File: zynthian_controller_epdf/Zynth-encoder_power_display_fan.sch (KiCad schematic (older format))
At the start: 41 parts, among them J3 40HAT, Q1 DMG2305UX, Q2 DMMT5401, Q3 AOD4184A, U2 CAT24C32, U3 MCP23017_SS

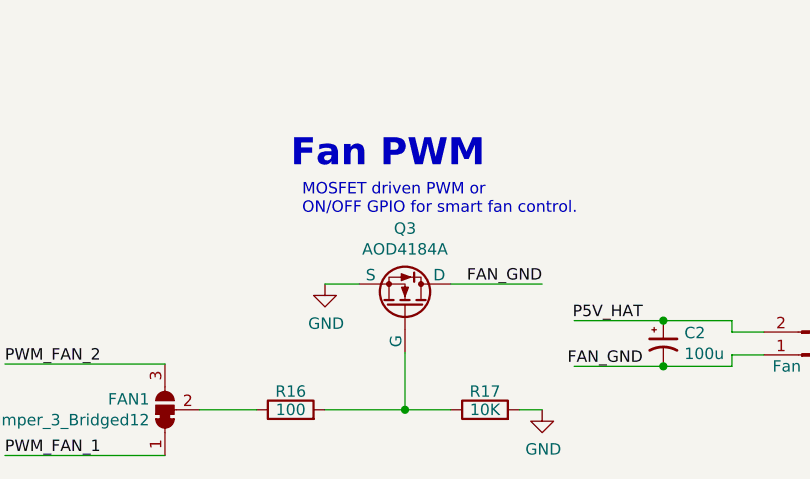
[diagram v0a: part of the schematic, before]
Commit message: Corrections before production.
Optimized and tested for submit
Manually corrected R12,18,19 as well as pin 1 orientations.
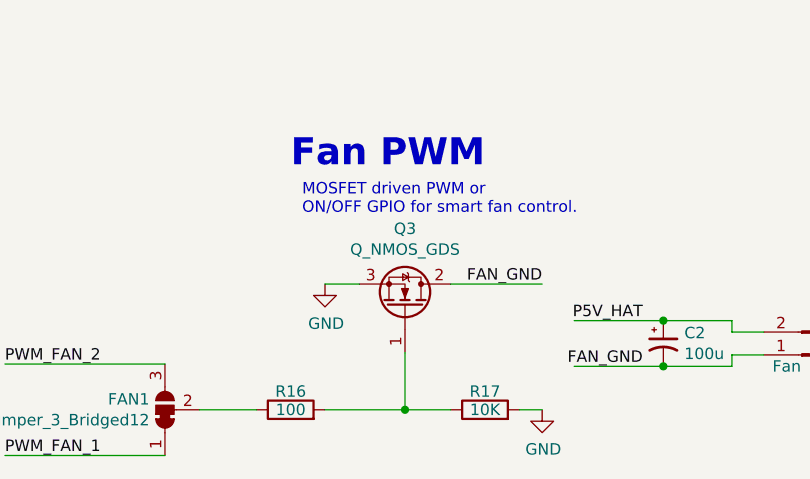
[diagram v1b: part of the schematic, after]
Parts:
- removed Q3: AOD4184A, Package_TO_SOT_SMD:TO-252-2, symbol Transistor_FET:AOD4184A
- added Q3: Q_NMOS_GDS, Package_TO_SOT_SMD:TO-252-2, symbol Device:Q_NMOS_GDS
- C2: footprint Capacitor_Tantalum_SMD:CP_EIA-7343-30_AVX-N -> Capacitor_Tantalum_SMD:CP_EIA-3528-15_AVX-H; LCSC C139578 -> C16133
- D5: LCSC C72044 -> C2286; MFG PART 19-217/R6C-AL1M2VY/3T -> (none)
- R10, R15, R17: LCSC C167144 -> C25804
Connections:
- net FAN_GND: now also Q3.2 (D)
- net GND: now also Q3.3 (S)
- net at R16.2, R17.1: now also Q3.1 (G)

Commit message: Final Changes before production
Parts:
- added R20: 100K, Resistor_SMD:R_0603_1608Metric, symbol Device:R
- C1: MFG PART CC0603KRX7R9BB104 -> (none)
- C2: MFG PART 20TQC100MYF -> (none)
- H5, H6: Field4 Pi Zero Mounting Hole -> (none)
- PWR1: Name ACC1 -> (none)
- PWR2: Name DSPL_PWR -> (none)
- PWR3: Name Fan -> (none)
- Q1: MFG PART DMG2305UX-13 -> (none)
- Q2: MFG PART DMMT5401-7-F -> (none)
- R10, R15, R17: MFG PART 0603WAD1002T5E -> (none)
- R11: footprint Resistor_SMD:R_0402_1005Metric -> Resistor_SMD:R_0603_1608Metric; LCSC C25792 -> C25819; MFG PART 0402WGF4702TCE -> (none)
- R12: MFG PART 0603WAF1001T5E -> (none)
- R13, R14: MFG PART 0603WAF3901T5E -> (none)
- R16: MFG PART 0805W8F1000T5E -> (none)
- R18, R19: value 1k -> 1K; MFG PART 0603WAF1001T5E -> (none)
- SJ1: Field4 EEPROM Write Enable -> (none)
- U2: MFG PART CAT24C32WI-GT3 -> (none)
- U3: MFG PART MCP23017-E/SO -> (none)
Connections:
- net E1+: now also R20.1
- net GND: now also R20.2
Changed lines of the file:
@@
 F 3 "https://datasheet.lcsc.com/szlcsc/Uniroyal-Elec-0603WAF1001T5E_C21190.pdf" H 6130 2400 50  0001 C CNN
 F 4 "C144153" H 6130 2400 50  0001 C CNN "LCSC"
-F 5 "DMG2305UX-13" H 6130 2400 50  0001 C CNN "MFG PART"
 	1    6130 2400
 	0    -1   -1   0
@@
 F 3 "https://datasheet.lcsc.com/szlcsc/Diodes-Incorporated-DMMT5401-7-F_C154733.pdf" H 5830 3000 50  0001 L CNN
 F 4 "C154733" H 5830 3000 50  0001 C CNN "LCSC"
-F 5 "DMMT5401-7-F" H 5830 3000 50  0001 C CNN "MFG PART"
 	1    5830 3000
 	-1   0    0    1
@@
 F 3 "https://datasheet.lcsc.com/szlcsc/Diodes-Incorporated-DMMT5401-7-F_C154733.pdf" H 6430 3000 50  0001 L CNN
 F 4 "C154733" H 6430 3000 50  0001 C CNN "LCSC"
-F 5 "DMMT5401-7-F" H 6430 3000 50  0001 C CNN "MFG PART"
 	2    6430 3000
 	1    0    0    1
@@
 F 3 "https://datasheet.lcsc.com/szlcsc/1811062009_UNI-ROYAL-Uniroyal-Elec-0603WAF1002T5E_C25804.pdf" H 5730 3600 50  0001 C CNN
 F 4 "C25804" H 5730 3600 50  0001 C CNN "LCSC"
-F 5 "0603WAD1002T5E" H 5730 3600 50  0001 C CNN "MFG PART"
 	1    5730 3600
 	1    0    0    -1
@@
 F 1 "5V Power" H 11640 3140 50  0001 C CNN
 F 2 "Connector_Wire:SolderWirePad_1x02_P5.08mm_Drill1.5mm" H 11390 3040 50  0001 C CNN
-F 3 "https://www.te.com/commerce/DocumentDelivery/DDEController?Action=srchrtrv&DocNm=63951&DocType=Customer+Drawing&DocLang=English" H 11390 3040 50  0001 C CNN
+F 3 "~" H 11390 3040 50  0001 C CNN
 	1    11390 3040
 	-1   0    0    -1
@@
 F 1 "GND" H 11640 1990 50  0001 R CNN
 F 2 "Connector_Wire:SolderWirePad_1x02_P5.08mm_Drill1.5mm" H 11390 2190 50  0001 C CNN
-F 3 "https://www.te.com/commerce/DocumentDelivery/DDEController?Action=srchrtrv&DocNm=63951&DocType=Customer+Drawing&DocLang=English" H 11390 2190 50  0001 C CNN
+F 3 "~" H 11390 2190 50  0001 C CNN
 	1    11390 2190
 	-1   0    0    1
@@
 F 0 "R11" V 6610 3600 50  0000 C CNN
 F 1 "47K" V 6530 3600 50  0000 C CNN
-F 2 "Resistor_SMD:R_0402_1005Metric" V 6460 3600 50  0001 C CNN
-F 3 "https://datasheet.lcsc.com/szlcsc/Uniroyal-Elec-0402WGF4702TCE_C25792.pdf" H 6530 3600 50  0001 C CNN
-F 4 "C25792" H 6530 3600 50  0001 C CNN "LCSC"
-F 5 "0402WGF4702TCE" H 6530 3600 50  0001 C CNN "MFG PART"
+F 2 "Resistor_SMD:R_0603_1608Metric" V 6460 3600 50  0001 C CNN
+F 3 "https://datasheet.lcsc.com/szlcsc/Uniroyal-Elec-0603WAF4702T5E_C25819.pdf" H 6530 3600 50  0001 C CNN
+F 4 "C25819" H 6530 3600 50  0001 C CNN "LCSC"
 	1    6530 3600
 	1    0    0    -1
@@
 F 3 "https://datasheet.lcsc.com/szlcsc/Uniroyal-Elec-0603WAF1001T5E_C21190.pdf" H 9990 2390 50  0001 C CNN
 F 4 "C21190" H 9990 2390 50  0001 C CNN "LCSC"
-F 5 "0603WAF1001T5E" H 9990 2390 50  0001 C CNN "MFG PART"
 	1    9990 2390
 	1    0    0    1
@@
 F 2 "Jumper:SolderJumper-2_P1.3mm_Open_RoundedPad1.0x1.5mm" H 940 6030 50  0001 C CNN
 F 3 "~" H 940 6030 50  0001 C CNN
-F 4 "EEPROM Write Enable" V 810 5540 50  0000 C CNN "Field4"
 	1    940  6030
 	0    -1   -1   0
@@
 F 3 "https://datasheet.lcsc.com/szlcsc/Uniroyal-Elec-0603WAF3901T5E_C23018.pdf" H 3030 7450 50  0001 C CNN
 F 4 "C23018" H 3030 7450 50  0001 C CNN "LCSC"
-F 5 "0603WAF3901T5E" H 3030 7450 50  0001 C CNN "MFG PART"
 	1    3030 7450
 	0    1    1    0
@@
 F 3 "https://datasheet.lcsc.com/szlcsc/Uniroyal-Elec-0603WAF3901T5E_C23018.pdf" H 3030 7200 50  0001 C CNN
 F 4 "C23018" H 3030 7200 50  0001 C CNN "LCSC"
-F 5 "0603WAF3901T5E" H 3030 7200 50  0001 C CNN "MFG PART"
 	1    3030 7200
 	0    1    1    0
@@
 F 3 "https://datasheet.lcsc.com/szlcsc/ON-Semicon-ON-CAT24C32WI-GT3_C81193.pdf" H 2620 5680 50  0001 C CNN
 F 4 "C81193" H 2620 5680 50  0001 C CNN "LCSC"
-F 5 "CAT24C32WI-GT3" H 2620 5680 50  0001 C CNN "MFG PART"
 	1    2620 5680
 	1    0    0    -1
@@
 F 2 "project_footprints:NPTH_3mm_ID" H 12660 3010 60  0001 C CNN
 F 3 "~" H 12660 3010 60  0001 C CNN
-F 4 "Pi Zero Mounting Hole" H 12750 2760 50  0000 C CNN "Field4"
 	1    12760 3010
 	1    0    0    -1
@@
 F 2 "project_footprints:NPTH_3mm_ID" H 13710 3010 60  0001 C CNN
 F 3 "~" H 13710 3010 60  0001 C CNN
-F 4 "Pi Zero Mounting Hole" H 13800 2760 50  0000 C CNN "Field4"
 	1    13810 3010
 	1    0    0    -1
@@
 F 3 "https://datasheet.lcsc.com/szlcsc/1811071223_AVX-TAJB107K006RNJ_C16133.pdf" H 4120 9470 50  0001 C CNN
 F 4 "C16133" H 4120 9470 50  0001 C CNN "LCSC"
-F 5 "20TQC100MYF" H 4120 9470 50  0001 C CNN "MFG PART"
 	1    4120 9470
 	1    0    0    -1
@@
 F 3 "https://datasheet.lcsc.com/szlcsc/1811062009_UNI-ROYAL-Uniroyal-Elec-0603WAF1002T5E_C25804.pdf" H 3340 9760 50  0001 C CNN
 F 4 "C25804" H 3340 9760 50  0001 C CNN "LCSC"
-F 5 "0603WAD1002T5E" H 3340 9760 50  0001 C CNN "MFG PART"
 	1    3340 9760
 	0    -1   -1   0
@@
 F 2 "Connector_JST:JST_XH_B2B-XH-A_1x02_P2.50mm_Vertical" H 4760 9520 50  0001 C CNN
 F 3 "~" H 4760 9520 50  0001 C CNN
-F 4 "Fan" H 4860 9570 50  0000 C CNN "Name"
 	1    4760 9520
 	-1   0    0    1
@@
 F 2 "Connector_JST:JST_XH_B2B-XH-A_1x02_P2.50mm_Vertical" H 10540 3920 50  0001 C CNN
 F 3 "~" H 10540 3920 50  0001 C CNN
-F 4 "DSPL_PWR" H 10790 4020 50  0000 C CNN "Name"
 	1    10540 3920
 	-1   0    0    1
@@
 F 3 "https://datasheet.lcsc.com/szlcsc/1811062009_UNI-ROYAL-Uniroyal-Elec-0603WAF1002T5E_C25804.pdf" H 2070 6230 50  0001 C CNN
 F 4 "C25804" H 2070 6230 50  0001 C CNN "LCSC"
-F 5 "0603WAD1002T5E" H 2070 6230 50  0001 C CNN "MFG PART"
 	1    2070 6230
 	-1   0    0    1
@@
 Text Label 12330 7000 2    50   ~ 0
 GSW2
-$Comp
-L Device:R R18
-U 1 1 5E20EC4C
-P 12330 8250
-F 0 "R18" V 12230 8250 50  0000 C CNN
-F 1 "1k" V 12330 8250 50  0000 C CNN
-F 2 "Resistor_SMD:R_0603_1608Metric" V 12260 8250 50  0001 C CNN
-F 3 "https://datasheet.lcsc.com/szlcsc/Uniroyal-Elec-0603WAF1001T5E_C21190.pdf" H 12330 8250 50  0001 C CNN
-F 4 "C21190" H 12330 8250 50  0001 C CNN "LCSC"
-F 5 "0603WAF1001T5E" H 12330 8250 50  0001 C CNN "MFG PART"
-	1    12330 8250
-	0    1    1    0
-$EndComp
-$Comp
-L Interface_Expansion:MCP23017_SS U3
-U 1 1 5E01D4F6
-P 11280 7100
-F 0 "U3" H 11280 8381 50  0000 C CNN
-F 1 "MCP23017_SS" H 11280 8290 50  0000 C CNN
-F 2 "Package_SO:SOIC-28W_7.5x17.9mm_P1.27mm" H 11480 6100 50  0001 L CNN
-F 3 "http://ww1.microchip.com/downloads/en/DeviceDoc/20001952C.pdf" H 11480 6000 50  0001 L CNN
-F 4 "C47023" H 11280 7100 50  0001 C CNN "LCSC"
-F 5 "MCP23017-E/SO" H 11280 7100 50  0001 C CNN "MFG PART"
-	1    11280 7100
-	1    0    0    -1
-$EndComp
 Text Notes 9270 6940 0    50   ~ 0
 I2C Addr: \n          A0   A1   A2\n0x20: 1-2  1-2  1-2\n0x21: 2-3  1-2  1-2\n0x22: 1-2  2-3  1-2\n0x23: 2-3  2-3  1-2\n\n
@@
 F 3 "https://datasheet.lcsc.com/szlcsc/YAGEO-CC0603KRX7R9BB104_C14663.pdf" H 11780 5900 50  0001 C CNN
 F 4 "C14663" H 11780 5900 50  0001 C CNN "LCSC"
-F 5 "CC0603KRX7R9BB104" H 11780 5900 50  0001 C CNN "MFG PART"
 	1    11780 5900
 	1    0    0    -1
@@
 F 2 "Connector_JST:JST_XH_B4B-XH-A_1x04_P2.50mm_Vertical" H 7320 5730 50  0001 C CNN
 F 3 "~" H 7320 5730 50  0001 C CNN
-F 4 "ACC1" H 7420 5920 50  0000 C CNN "Name"
 	1    7320 5730
 	-1   0    0    1
@@
 P 6120 5680
 F 0 "R19" V 6220 5660 50  0000 C CNN
-F 1 "1k" V 6120 5680 50  0000 C CNN
+F 1 "1K" V 6120 5680 50  0000 C CNN
 F 2 "Resistor_SMD:R_0603_1608Metric" V 6050 5680 50  0001 C CNN
 F 3 "https://datasheet.lcsc.com/szlcsc/Uniroyal-Elec-0603WAF1001T5E_C21190.pdf" H 6120 5680 50  0001 C CNN
 F 4 "C21190" H 6120 5680 50  0001 C CNN "LCSC"
-F 5 "0603WAF1001T5E" H 6120 5680 50  0001 C CNN "MFG PART"
 	1    6120 5680
 	0    1    1    0
@@
 F 3 "https://datasheet.lcsc.com/szlcsc/Uniroyal-Elec-0805W8F1000T5E_C17408.pdf" H 2490 9760 50  0001 C CNN
 F 4 "C17408" H 2490 9760 50  0001 C CNN "LCSC"
-F 5 "0805W8F1000T5E" H 2490 9760 50  0001 C CNN "MFG PART"
 	1    2490 9760
 	0    -1   -1   0
 $EndComp
+$Comp
+L Interface_Expansion:MCP23017_SS U3
+U 1 1 5E01D4F6
+P 11280 7100
+F 0 "U3" H 11280 8381 50  0000 C CNN
+F 1 "MCP23017_SS" H 11280 8290 50  0000 C CNN
+F 2 "Package_SO:SOIC-28W_7.5x17.9mm_P1.27mm" H 11480 6100 50  0001 L CNN
+F 3 "http://ww1.microchip.com/downloads/en/DeviceDoc/20001952C.pdf" H 11480 6000 50  0001 L CNN
+F 4 "C47023" H 11280 7100 50  0001 C CNN "LCSC"
+	1    11280 7100
+	1    0    0    -1
+$EndComp
+$Comp
+L Device:R R20
+U 1 1 5E66F556
+P 12330 8390
+F 0 "R20" V 12420 8390 50  0000 C CNN
+F 1 "100K" V 12330 8390 50  0000 C CNN
+F 2 "Resistor_SMD:R_0603_1608Metric" V 12260 8390 50  0001 C CNN
+F 3 "https://datasheet.lcsc.com/szlcsc/1810201809_UNI-ROYAL-Uniroyal-Elec-0603WAF1003T5E_C25803.pdf" H 12330 8390 50  0001 C CNN
+F 4 "C25803" V 12330 8390 50  0001 C CNN "LCSC"
+	1    12330 8390
+	0    1    1    0
+$EndComp
+$Comp
+L Device:R R18
+U 1 1 5E20EC4C
+P 12330 8250
+F 0 "R18" V 12230 8250 50  0000 C CNN
+F 1 "1K" V 12330 8250 50  0000 C CNN
+F 2 "Resistor_SMD:R_0603_1608Metric" V 12260 8250 50  0001 C CNN
+F 3 "https://datasheet.lcsc.com/szlcsc/Uniroyal-Elec-0603WAF1001T5E_C21190.pdf" H 12330 8250 50  0001 C CNN
+F 4 "C21190" H 12330 8250 50  0001 C CNN "LCSC"
+	1    12330 8250
+	0    1    1    0
+$EndComp
+Wire Wire Line
+	12480 8390 12480 8250
+Connection ~ 12480 8250
+Wire Wire Line
+	12180 8390 11830 8390
+Text Label 11830 8390 0    50   ~ 0
+GND
 $EndSCHEMATC

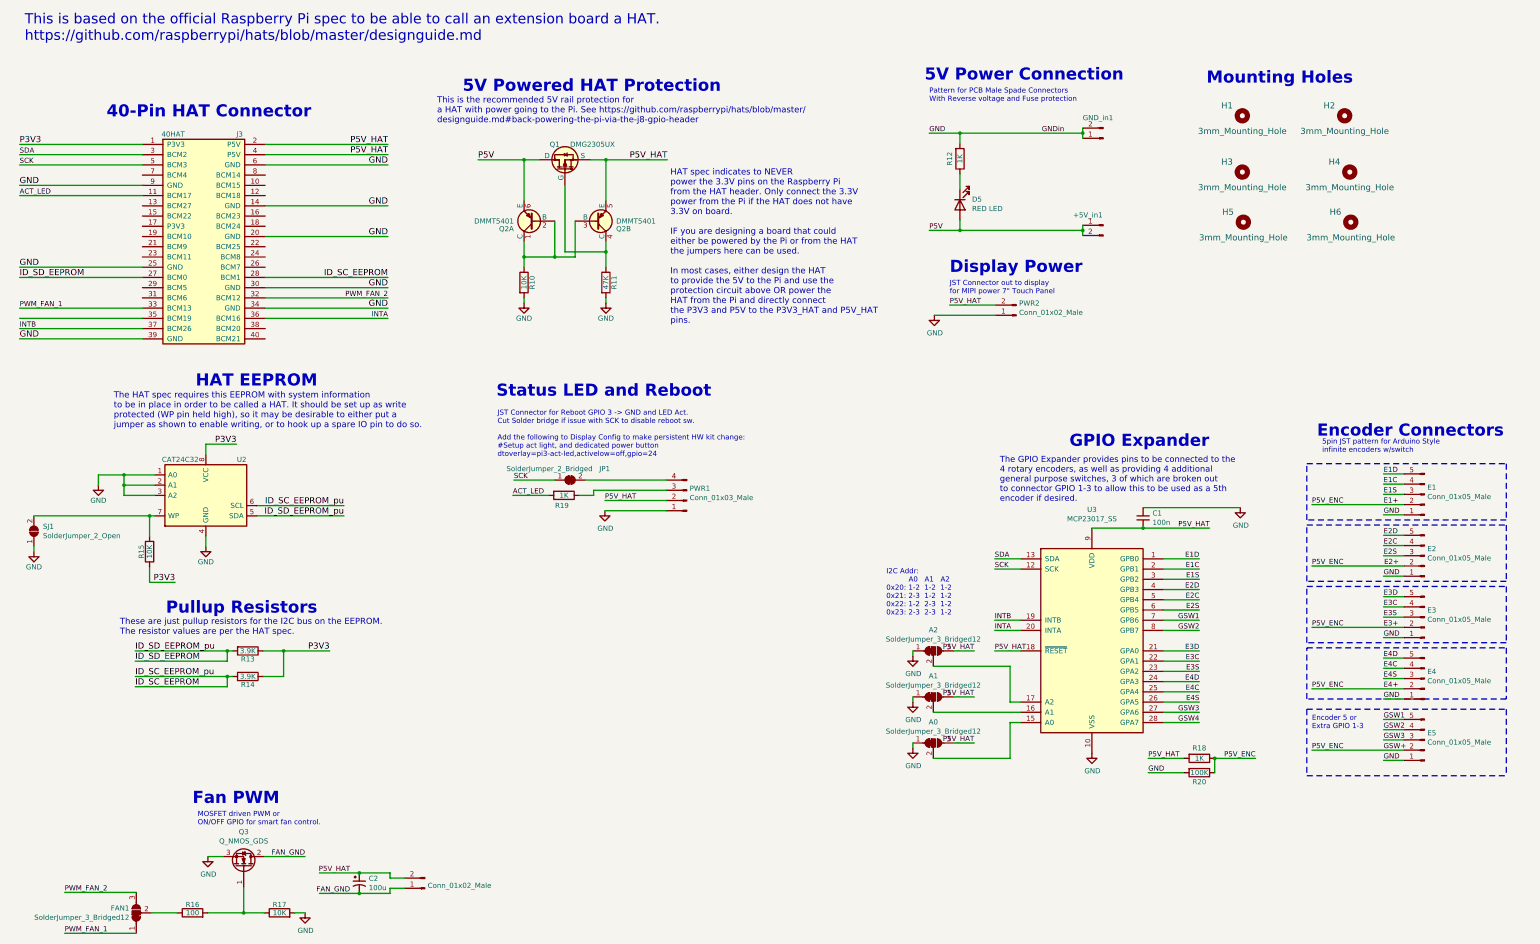
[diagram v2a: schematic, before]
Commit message: Move GPIOs change act_led R19 220 Ohm
Based upon various descriptions of Pi LED, and 3.3V Decided to use
220 Ohm resistor, rather than 0Ohm or 1K. 603 pad is possible to
replace resistor if required. Should be low enough R to work on all LED

Rework GPIO lines to use lines marked not in use by Ozz display in
hopes of keeping this compatible for most folks.

It will be possible to mag wire rework and epoxy glue to do a test
upgrade before the next rev of HW. Should even be clean and tidy.
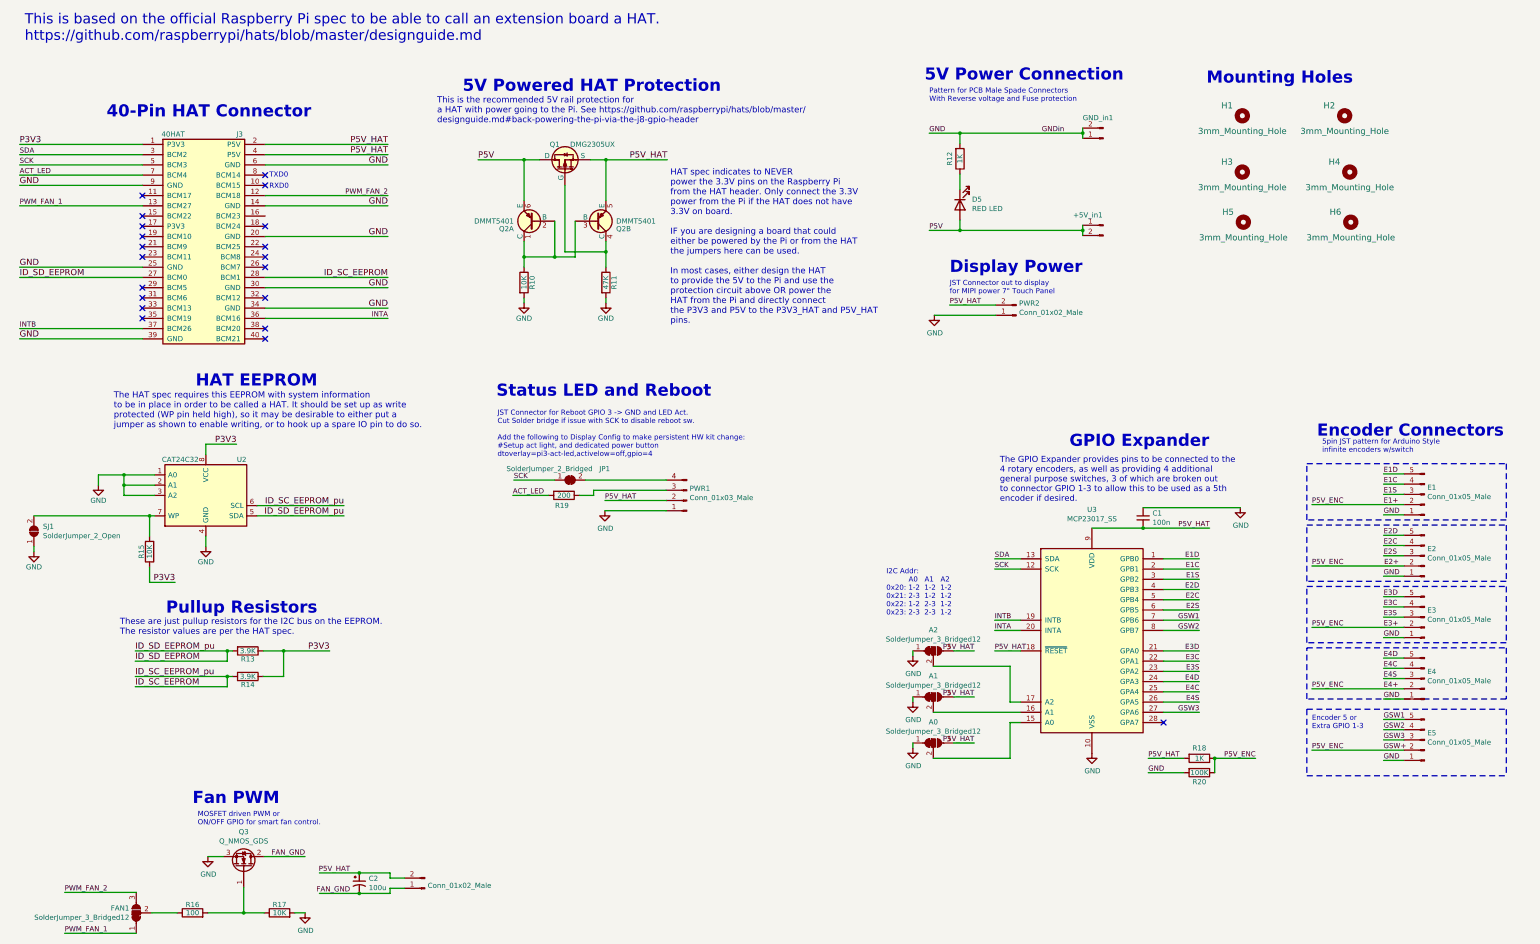
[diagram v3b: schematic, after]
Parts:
- R19: value 1K -> 200; LCSC C21190 -> C25217
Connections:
- net ACT_LED: now also J3.7 (BCM4); no longer J3.11 (BCM17)
- net PWM_FAN_1: now also J3.13 (BCM27); no longer J3.33 (BCM13)
- net PWM_FAN_2: now also J3.12 (BCM18); no longer J3.32 (BCM12)
- net GSW4: no longer names the net of U3.28 (GPA7)
- no-connect marks 0 -> 20
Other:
- note added: "JST Connector for Reboot GPIO 3 -> GND and LED Act.\nCut Solder bridge if issue with SCK to disable reboot sw.\n\nAdd the following to Display Config to make persistent HW kit change:\n#Setup act light, and dedicated power button\ndtoverlay=pi3-act-led,activelow=off,gpio=4\n"
- note added: "RXD0"
- note added: "TXD0"
- note removed: "JST Connector for Reboot GPIO 3 -> GND and LED Act.\nCut Solder bridge if issue with SCK to disable reboot sw.\n\nAdd the following to Display Config to make persistent HW kit change:\n#Setup act light, and dedicated power button\ndtoverlay=pi3-act-led,activelow=off,gpio=24\n"
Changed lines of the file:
@@
 Text Notes 9690 1840 0    50   ~ 0
 Pattern for PCB Male Spade Connectors\nWith Reverse voltage and Fuse protection
-Text Label 800  3850 0    50   ~ 0
+Text Label 800  2850 0    50   ~ 0
 PWM_FAN_1
 Wire Wire Line
-	800  3850 2000 3850
+	800  2850 2000 2850
 Connection ~ 6530 3300
 Wire Wire Line
@@
 Text Label 1240 9960 0    50   ~ 0
 PWM_FAN_1
-Text Label 4400 3750 2    50   ~ 0
+Text Label 4400 2750 2    50   ~ 0
 PWM_FAN_2
 Wire Wire Line
-	4400 3750 3200 3750
+	4400 2750 3200 2750
 Text Label 10790 2140 0    50   ~ 0
 GNDin
@@
 	9990 2240 9990 2140
 Connection ~ 9990 2140
-Wire Wire Line
-	2000 3950 800  3950
 Connection ~ 11190 3090
 Wire Wire Line
@@
 Text Label 11830 8250 0    50   ~ 0
 P5V_HAT
-Text Label 12330 7900 2    50   ~ 0
-GSW4
-Wire Wire Line
-	12330 7900 11980 7900
 Text Label 12330 7800 2    50   ~ 0
 GSW3
@@
 Text Notes 5460 4730 0    118  ~ 24
 Status LED and Reboot
-Text Notes 5470 5310 0    50   ~ 0
-JST Connector for Reboot GPIO 3 -> GND and LED Act.\nCut Solder bridge if issue with SCK to disable reboot sw.\n\nAdd the following to Display Config to make persistent HW kit change:\n#Setup act light, and dedicated power button\ndtoverlay=pi3-act-led,activelow=off,gpio=24\n
 $Comp
 L power:GND #PWR0109
@@
 $EndComp
 Wire Wire Line
-	800  2750 2000 2750
-Text Label 800  2750 0    50   ~ 0
+	800  2550 2000 2550
+Text Label 800  2550 0    50   ~ 0
 ACT_LED
 $Comp
@@
 P 6120 5680
 F 0 "R19" V 6220 5660 50  0000 C CNN
-F 1 "1K" V 6120 5680 50  0000 C CNN
+F 1 "200" V 6120 5680 50  0000 C CNN
 F 2 "Resistor_SMD:R_0603_1608Metric" V 6050 5680 50  0001 C CNN
-F 3 "https://datasheet.lcsc.com/szlcsc/Uniroyal-Elec-0603WAF1001T5E_C21190.pdf" H 6120 5680 50  0001 C CNN
-F 4 "C21190" H 6120 5680 50  0001 C CNN "LCSC"
+F 3 "https://datasheet.lcsc.com/szlcsc/1811081715_UNI-ROYAL-Uniroyal-Elec-0603WAJ0201T5E_C25217.pdf" H 6120 5680 50  0001 C CNN
+F 4 "C25217" H 6120 5680 50  0001 C CNN "LCSC"
 	1    6120 5680
 	0    1    1    0
@@
 Text Label 11830 8390 0    50   ~ 0
 GND
+NoConn ~ 2000 3950
+NoConn ~ 3200 4150
+NoConn ~ 3200 4050
+NoConn ~ 3200 3450
+NoConn ~ 3200 3350
+NoConn ~ 3200 3250
+NoConn ~ 3200 3050
+NoConn ~ 3200 2650
+NoConn ~ 3200 2550
+NoConn ~ 2000 3750
+NoConn ~ 2000 3650
+NoConn ~ 2000 3350
+NoConn ~ 2000 3250
+NoConn ~ 2000 3150
+NoConn ~ 2000 3050
+NoConn ~ 2000 2950
+NoConn ~ 11980 7900
+Text Notes 3240 2580 0    50   ~ 0
+TXD0
+Text Notes 3240 2690 0    50   ~ 0
+RXD0
+NoConn ~ 2000 2750
+NoConn ~ 2000 3850
+NoConn ~ 3200 3750
+Text Notes 5470 5310 0    50   ~ 0
+JST Connector for Reboot GPIO 3 -> GND and LED Act.\nCut Solder bridge if issue with SCK to disable reboot sw.\n\nAdd the following to Display Config to make persistent HW kit change:\n#Setup act light, and dedicated power button\ndtoverlay=pi3-act-led,activelow=off,gpio=4\n
 $EndSCHEMATC
